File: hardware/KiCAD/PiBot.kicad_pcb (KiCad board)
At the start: 2 copper layers, 112 x 87 mm, 179 parts, among them P1 BREAKOUT, P10 BREAKOUT, P11 BREAKOUT, P12 BREAKOUT, P2 CONN_02X05, P3 I2C_EXPANSION, P4 SPI_EXPANSION, P5 Feather-Adaper, P6 BREAKOUT, P7 BREAKOUT, P8 BREAKOUT, P9 BREAKOUT, SW1 SPST, SW2 SW_SPDT, SW3 SW_SPDT, SW4 SW_SPDT, SW5 SW_SPDT, U1 DMG2302U, U10 AH3772, U11 AH3772, U12 AH3772, U13 BH1745NUC, U14 BH1745NUC, U15 L3GD20H, U16 LSM303DLHCTR, U17 N-FET, U2 MKL03ZxxVFK4, U3 N-FET, U4 TPS63060, U5 MC33926PNB, U6 MC33926PNB, U7 Motor, U8 Motor, U9 AH3772

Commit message: Inital routing done!!!!!
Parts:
- C36, C37, C39, C4, C40, C41, C42, C43, C44, C45, C46, C47, C48, C5, C6, C7, C8, D3, D5, D7, JP2, JP3, PTC1, R10, R24, R29, R31, R4, R5, R7, R9, TP1, TP11, TP13, TP14, TP15, TP19, TP23, TP25, TP29, TP3, TP35, TP39, TP41, TP43, TP45, TP47, TP49, TP5, TP7, TP8, TP9, U13, U14, U15, U16, U2: moved to B.Cu
- moved C35 141.5 mm to (170.4, 111.3)
- moved TP7 137.1 mm to (136.8, 146.0)
- moved C33 136.3 mm to (170.4, 113.1)
- moved TP35 133.4 mm to (143.3, 128.6)
- moved TP13 132.3 mm to (147.1, 146.0)
- moved TP45 130.6 mm to (164.9, 132.0)
- moved C29 129.2 mm to (170.4, 114.3)
- moved TP49 125.8 mm to (150.3, 119.1)
- moved TP1 123.0 mm to (143.4, 146.1)
- moved TP37 116.9 mm to (125.4, 68.9)
- moved R24 111.7 mm to (152.6, 100.1), turned to 270 degrees
- moved R4 105.2 mm to (168.8, 49.3), turned to 180 degrees
- moved TP14 104.7 mm to (146.7, 135.3)
- moved TP3 102.5 mm to (163.3, 112.9)
- moved C32 101.6 mm to (121.0, 114.1), turned to 180 degrees
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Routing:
- net +3V3: track 181.6 -> 389.8 mm, vias 4 -> 13
- net SDA: track 0.00 -> 160.2 mm, vias 0 -> 9
- net SCL: track 0.00 -> 154.2 mm, vias 0 -> 7
- net PG: track 0.07 -> 143.0 mm, vias 0 -> 5
- net ~MotorR_D: track 0.00 -> 94.6 mm, vias 0 -> 5
- net rear_bumper: track 2.28 -> 92.3 mm, vias 0 -> 4
- net FB_L: track 0.00 -> 87.5 mm, vias 0 -> 6
- net front_bumper: track 0.00 -> 83.7 mm
- net ~MotorL_D: track 0.00 -> 82.6 mm, vias 0 -> 7
- net left_encB: track 3.50 -> 83.0 mm, vias 0 -> 6
- net right_encA: track 4.27 -> 80.9 mm, vias 0 -> 2
- net MotorL_Inv: track 0.00 -> 75.8 mm, vias 0 -> 6
- net left_encA: track 3.50 -> 78.5 mm, vias 0 -> 6
- net Net-(R29-Pad1): track 0.00 -> 74.7 mm
- net right_encB: track 4.05 -> 76.9 mm, vias 0 -> 6
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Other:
- board size 112 x 87 mm -> 112 x 117 mm

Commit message: Start of relayout
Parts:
- moved TP45 151.1 mm to (281.2, 35.6)
- moved TP3 142.9 mm to (276.3, 25.5)
- moved R24 135.5 mm to (262.5, 20.9)
- moved R20 133.8 mm to (276.4, 22.9)
- moved C21 133.5 mm to (276.3, 21.4)
- moved D12 133.1 mm to (276.1, 19.8)
- moved U6 132.2 mm to (269.7, 22.8)
- moved R18 132.1 mm to (274.4, 16.9)
- moved C35 131.5 mm to (273.4, 29.5)
- moved TP9 131.3 mm to (275.6, 37.1)
- moved C33 131.3 mm to (273.3, 31.5)
- moved C29 131.2 mm to (273.5, 33.1)
- moved R22 130.7 mm to (264.0, 20.8)
- moved TP19 130.4 mm to (265.5, 32.3)
- moved C18 129.9 mm to (263.6, 27.4)
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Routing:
- net +3V3: track 389.8 -> 0.00 mm, vias 13 -> 0
- net +BATT: track 243.1 -> 0.00 mm, vias 18 -> 0
- net GNDPWR: track 171.4 -> 0.00 mm, vias 8 -> 0
- net SDA: track 160.2 -> 0.00 mm, vias 9 -> 0
- net SCL: track 154.2 -> 0.00 mm, vias 7 -> 0
- net +5V: track 154.2 -> 0.00 mm, vias 4 -> 0
- net PG: track 143.0 -> 0.00 mm, vias 5 -> 0
- net ~MotorSF: track 118.1 -> 0.00 mm, vias 6 -> 0
- net ~MotorR_D: track 94.6 -> 0.00 mm, vias 5 -> 0
- net rear_bumper: track 92.3 -> 0.00 mm, vias 4 -> 0
- net FB_L: track 87.5 -> 0.00 mm, vias 6 -> 0
- net front_bumper: track 83.7 -> 0.00 mm
- net left_encB: track 83.0 -> 0.00 mm, vias 6 -> 0
- net ~MotorL_D: track 82.6 -> 0.00 mm, vias 7 -> 0
- net right_encA: track 80.9 -> 0.00 mm, vias 2 -> 0
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- removed copper zone on B.Cu, net GND
- removed copper zone on F.Cu, net GND
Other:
- board size 112 x 117 mm -> 64 x 123 mm

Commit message: Headway on schematic layout
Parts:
- removed P1: BREAKOUT, Pin_Headers:Pin_Header_Straight_1x07_Pitch2.54mm
- removed P10, P6, P9: BREAKOUT, Pin_Headers:Pin_Header_Straight_1x01_Pitch2.54mm
- removed P11, P8: BREAKOUT, Pin_Headers:Pin_Header_Straight_2x01_Pitch2.54mm
- removed P12: BREAKOUT, Pin_Headers:Pin_Header_Straight_1x03_Pitch2.54mm
- removed P4: SPI_EXPANSION, Pin_Headers:Pin_Header_Straight_1x03_Pitch2.54mm
- removed P7: BREAKOUT, Pin_Headers:Pin_Header_Straight_1x05_Pitch2.54mm
- added DRDY1: TEST, Measurement_Points:Measurement_Point_Round-SMD-Pad_Small, F.Cu at (148.0, 153.0)
- added INT1: TEST, Measurement_Points:Measurement_Point_Round-SMD-Pad_Small, F.Cu at (142.0, 153.0)
- added INT2: TEST, Measurement_Points:Measurement_Point_Round-SMD-Pad_Small, F.Cu at (145.0, 153.0)
- added TP10: TEST, Measurement_Points:Measurement_Point_Round-SMD-Pad_Small, F.Cu at (164.5, 163.8)
- added TP12: TEST, Measurement_Points:Measurement_Point_Round-SMD-Pad_Small, F.Cu at (142.5, 164.8)
- added TP4: TEST, Measurement_Points:Measurement_Point_Round-SMD-Pad_Small, F.Cu at (160.5, 161.8)
- added TP6: TEST, Measurement_Points:Measurement_Point_Round-SMD-Pad_Small, F.Cu at (148.5, 163.5)
- R8: moved to B.Cu
- moved TP33 135.9 mm to (126.0, 142.5)
- moved C45 134.1 mm to (149.9, 151.5), turned to 180 degrees
- moved R5 133.9 mm to (159.4, 148.2), turned to 90 degrees
- moved C44 133.4 mm to (151.2, 149.5), turned to 180 degrees
- moved U13 132.8 mm to (181.0, 150.5)
- moved U14 132.5 mm to (129.0, 150.5)
- moved C48 132.1 mm to (158.5, 153.1)
- moved U16 132.0 mm to (155.0, 151.5)
- moved R4 131.8 mm to (158.0, 146.6), turned to 0 degrees
- moved C39 131.7 mm to (179.5, 154.0)
- moved C36 130.7 mm to (125.5, 149.0)
- moved TP31 130.4 mm to (126.0, 136.5)
- moved C47 130.2 mm to (151.1, 153.5), turned to 180 degrees
- moved TP27 128.3 mm to (126.0, 139.5)
- moved R8 127.4 mm to (126.9, 134.7), turned to 270 degrees
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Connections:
- P2 pad 7: Net-(P2-Pad7) -> (no net)
- P2 pad 8: Net-(P2-Pad8) -> (no net)
- P5 pad 1: Net-(P5-Pad1) -> (no net)
- P5 pad 10: Net-(P1-Pad1) -> (no net)
- P5 pad 14: Net-(P5-Pad14) -> (no net)
- P5 pad 15: Net-(P5-Pad15) -> (no net)
- P5 pad 20: Net-(P5-Pad20) -> (no net)
- P5 pad 21: Net-(P5-Pad21) -> (no net)
- P5 pad 22: Net-(P5-Pad22) -> (no net)
- P5 pad 23: Net-(P5-Pad23) -> (no net)
- P5 pad 24: Net-(P5-Pad24) -> (no net)
- P5 pad 26: Net-(P5-Pad26) -> (no net)
- P5 pad 4: Net-(P1-Pad7) -> (no net)
- P5 pad 5: Net-(P1-Pad6) -> (no net)
- P5 pad 6: Net-(P1-Pad5) -> (no net)
- P5 pad 7: Net-(P1-Pad4) -> (no net)
- P5 pad 8: Net-(P1-Pad3) -> (no net)
- P5 pad 9: Net-(P1-Pad2) -> (no net)
- SD1 pad PIN8: Net-(SD1-PadPIN8) -> (no net)
- SW2 pad 1: Net-(SW2-Pad1) -> (no net)
- SW3 pad 1: Net-(SW3-Pad1) -> (no net)
- SW4 pad 1: Net-(SW4-Pad1) -> (no net)
- SW5 pad 1: Net-(SW5-Pad1) -> (no net)
- TP25 pad 1: MotorR_Inv -> (no net)
- U13 pad 8: Net-(U13-Pad8) -> (no net)
- U14 pad 8: Net-(U14-Pad8) -> (no net)
- U16 pad 8: Net-(U16-Pad8) -> (no net)
- U5 pad 17: Net-(U5-Pad17) -> (no net)
- U5 pad 25: Net-(U5-Pad25) -> (no net)
- U5 pad 3: Net-(U5-Pad3) -> (no net)
- U5 pad 9: Net-(U5-Pad9) -> (no net)
- U6 pad 17: Net-(U6-Pad17) -> (no net)
- U6 pad 25: Net-(U6-Pad25) -> (no net)
- U6 pad 3: Net-(U6-Pad3) -> (no net)
- U6 pad 7: /motors/MotorR_Inv -> (no net)
- U6 pad 9: Net-(U6-Pad9) -> (no net)
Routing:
- net SCK: track 0.00 -> 27.5 mm, vias 0 -> 3
- net MISO: track 0.00 -> 24.6 mm, vias 0 -> 3
- net MOSI: track 0.00 -> 23.1 mm, vias 0 -> 3
- net Net-(DRDY1-Pad1): track 0.00 -> 21.1 mm, vias 0 -> 1
- net Net-(JP1-Pad1): track 0.00 -> 17.9 mm, vias 0 -> 1
- net Net-(SD1-PadPIN1): track 0.00 -> 17.8 mm, vias 0 -> 2
- net Net-(INT1-Pad1): track 0.00 -> 14.7 mm, vias 0 -> 1
- net Net-(INT2-Pad1): track 0.00 -> 10.9 mm, vias 0 -> 1
- net +3V3: track 0.00 -> 9.91 mm
- net SD_CS: track 0.00 -> 7.12 mm, vias 0 -> 2
- net Net-(C48-Pad1): track 0.00 -> 2.52 mm
- net Net-(C48-Pad2): track 0.00 -> 2.52 mm
- net Net-(C44-Pad1): track 0.00 -> 2.30 mm
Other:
- net class any added: clearance 0, trace_width 0.3, via_dia 0.6, via_drill 0.4
- board text added: "MISO"
- board text added: "MOSI"
- board text added: "SCK"
- board text added: "SD_CS"

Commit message: Lay out encoders and begin motor drive
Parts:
- C24, C25, C28, C29, C30, C31, C32, C33, C34, C35, U5, U6: moved to B.Cu
- JP10, JP11, JP12, JP13, JP14, JP7, JP8, JP9: moved to F.Cu
- moved C27 132.6 mm to (155.0, 40.5), turned to 90 degrees
- moved JP9 129.7 mm to (157.0, 38.0), turned to 270 degrees
- moved JP14 126.1 mm to (157.0, 40.5), turned to 90 degrees
- moved R27 121.9 mm to (156.0, 42.5)
- moved R25 121.4 mm to (156.0, 52.5)
- moved JP10 121.3 mm to (157.0, 57.0)
- moved U10 120.9 mm to (157.0, 50.0)
- moved JP12 120.8 mm to (157.0, 54.5), turned to 270 degrees
- moved U5 119.6 mm to (129.5, 47.5), turned to 180 degrees
- moved U12 118.4 mm to (157.0, 45.0)
- moved C23 114.6 mm to (163.5, 40.5), turned to 0 degrees
- moved C31 113.5 mm to (164.5, 47.0), turned to 270 degrees
- moved C25 112.5 mm to (163.0, 47.0), turned to 270 degrees
- moved JP13 112.3 mm to (153.0, 40.5), turned to 90 degrees
- moved JP7 106.8 mm to (153.0, 38.0)
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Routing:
- net +3V3: track 9.91 -> 47.6 mm, vias 0 -> 2
- net Net-(BT3-Pad2): track 0.00 -> 30.2 mm
- net Net-(BT2-Pad2): track 0.00 -> 30.2 mm
- net Net-(BT1-Pad2): track 0.00 -> 30.2 mm
- net /power/BATT_V+_TERM: track 0.00 -> 26.0 mm
- net Net-(C22-Pad2): track 0.00 -> 21.0 mm
- net Net-(C23-Pad2): track 0.00 -> 21.0 mm
- net Net-(JP8-Pad2): track 0.00 -> 17.2 mm, vias 0 -> 2
- net Net-(JP7-Pad1): track 0.00 -> 15.6 mm, vias 0 -> 2
- net Net-(JP9-Pad1): track 0.00 -> 14.6 mm, vias 0 -> 2
- net Net-(JP10-Pad2): track 0.00 -> 11.2 mm, vias 0 -> 2
- net Net-(R32-Pad1): track 0.00 -> 10.5 mm
- net /power/BATT_GND_TERM: track 0.00 -> 7.62 mm
- net Net-(C23-Pad1): track 0.00 -> 5.86 mm
- net Net-(C22-Pad1): track 0.00 -> 5.86 mm
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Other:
- net class any removed

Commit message: Lay out motor drivers
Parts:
- C20, C21, D11, D12, JP5, R17, R18, TP11, TP19, TP3, TP39, TP9: moved to F.Cu
- moved JP17 169.3 mm to (164.0, 69.0), turned to 90 degrees
- moved TP9 108.1 mm to (167.5, 35.0)
- moved TP11 105.6 mm to (165.0, 35.0)
- moved TP3 91.7 mm to (145.0, 35.0)
- moved TP19 60.6 mm to (213.5, 101.5)
- moved D12 40.2 mm to (174.5, 60.0), turned to 270 degrees
- moved R19 39.9 mm to (142.5, 51.5), turned to 0 degrees
- moved R18 38.4 mm to (176.5, 60.0), turned to 270 degrees
- moved R20 37.8 mm to (173.5, 51.0), turned to 0 degrees
- moved R22 37.2 mm to (165.0, 59.5), turned to 270 degrees
- moved C20 36.8 mm to (147.0, 60.0), turned to 270 degrees
- moved C21 36.1 mm to (178.5, 60.0), turned to 270 degrees
- moved R21 34.2 mm to (134.0, 59.0)
- moved JP5 34.0 mm to (149.5, 60.0), turned to 90 degrees
- moved C18 33.1 mm to (165.0, 51.5)
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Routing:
- net Net-(C22-Pad2): track 21.0 -> 153.6 mm
- net Net-(C23-Pad1): track 5.86 -> 121.4 mm
- net GNDPWR: track 0.00 -> 82.3 mm
- net PG: track 0.00 -> 69.2 mm, vias 0 -> 4
- net +BATT: track 0.00 -> 68.4 mm
- net Motor_In1: track 0.00 -> 66.0 mm, vias 0 -> 4
- net Motor_In2: track 0.00 -> 63.1 mm, vias 0 -> 4
- net ~MotorSF: track 0.00 -> 36.0 mm, vias 0 -> 4
- net Net-(C23-Pad2): track 21.0 -> 52.9 mm
- net Net-(C22-Pad1): track 5.86 -> 36.0 mm
- net Net-(C20-Pad1): track 0.00 -> 15.3 mm, vias 0 -> 1
- net Net-(C21-Pad1): track 0.00 -> 12.7 mm, vias 0 -> 1
- net Net-(C18-Pad2): track 0.00 -> 3.43 mm
- net Net-(C19-Pad2): track 0.00 -> 2.72 mm
- net Net-(R22-Pad1): track 0.00 -> 2.09 mm
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- added copper zone on B.Cu, net +BATT
- added copper zone on B.Cu, net GNDPWR
- added copper zone on B.Cu, net Net-(C22-Pad1)
- added copper zone on B.Cu, net Net-(C22-Pad2)
- added copper zone on B.Cu, net Net-(C23-Pad1)
- added copper zone on B.Cu, net Net-(C23-Pad2)

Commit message: Layout PSU
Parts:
- moved D9 194.8 mm to (184.0, 82.5), turned to 270 degrees
- moved JP18 190.8 mm to (176.5, 71.0), turned to 270 degrees
- moved JP4 182.8 mm to (176.5, 76.5), turned to 270 degrees
- moved D8 181.6 mm to (184.0, 97.5)
- moved U17 167.1 mm to (172.5, 72.5), turned to 0 degrees
- moved R32 161.2 mm to (168.5, 72.5), turned to 90 degrees
- moved U3 159.1 mm to (172.5, 77.5), turned to 0 degrees
- moved C9 158.1 mm to (172.5, 75.0), turned to 0 degrees
- moved C10 156.1 mm to (165.5, 77.5)
- moved D10 155.7 mm to (168.5, 77.5), turned to 90 degrees
- moved C11 149.2 mm to (163.5, 114.0), turned to 270 degrees
- moved R11 140.7 mm to (167.5, 112.5), turned to 180 degrees
- moved C12 123.6 mm to (160.0, 114.0), turned to 270 degrees
- moved L1 119.5 mm to (154.5, 109.5), turned to 180 degrees
- moved R13 115.6 mm to (154.5, 118.0), turned to 0 degrees
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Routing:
- net Net-(R32-Pad1): track 10.5 -> 75.0 mm, vias 0 -> 1
- net /power/BATT_V+_TERM: track 26.0 -> 89.4 mm, vias 0 -> 2
- net /power/BATT_GND_TERM: track 7.62 -> 34.0 mm
- net /power/PSU_VOUT: track 0.00 -> 15.2 mm
- net +BATT: track 68.4 -> 82.6 mm
- net Net-(C9-Pad2): track 0.00 -> 11.8 mm
- net Net-(D8-Pad2): track 0.00 -> 11.0 mm
- net /power/PSU_FB: track 0.00 -> 8.06 mm
- net Net-(L1-Pad2): track 0.00 -> 3.64 mm
- net /power/PSU_IND: track 0.00 -> 3.64 mm
- net Net-(R12-Pad2): track 0.00 -> 2.78 mm
- added copper zone on B.Cu, net /power/PSU_VOUT
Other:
- net class Default: trace_width 0.4 -> 0.6

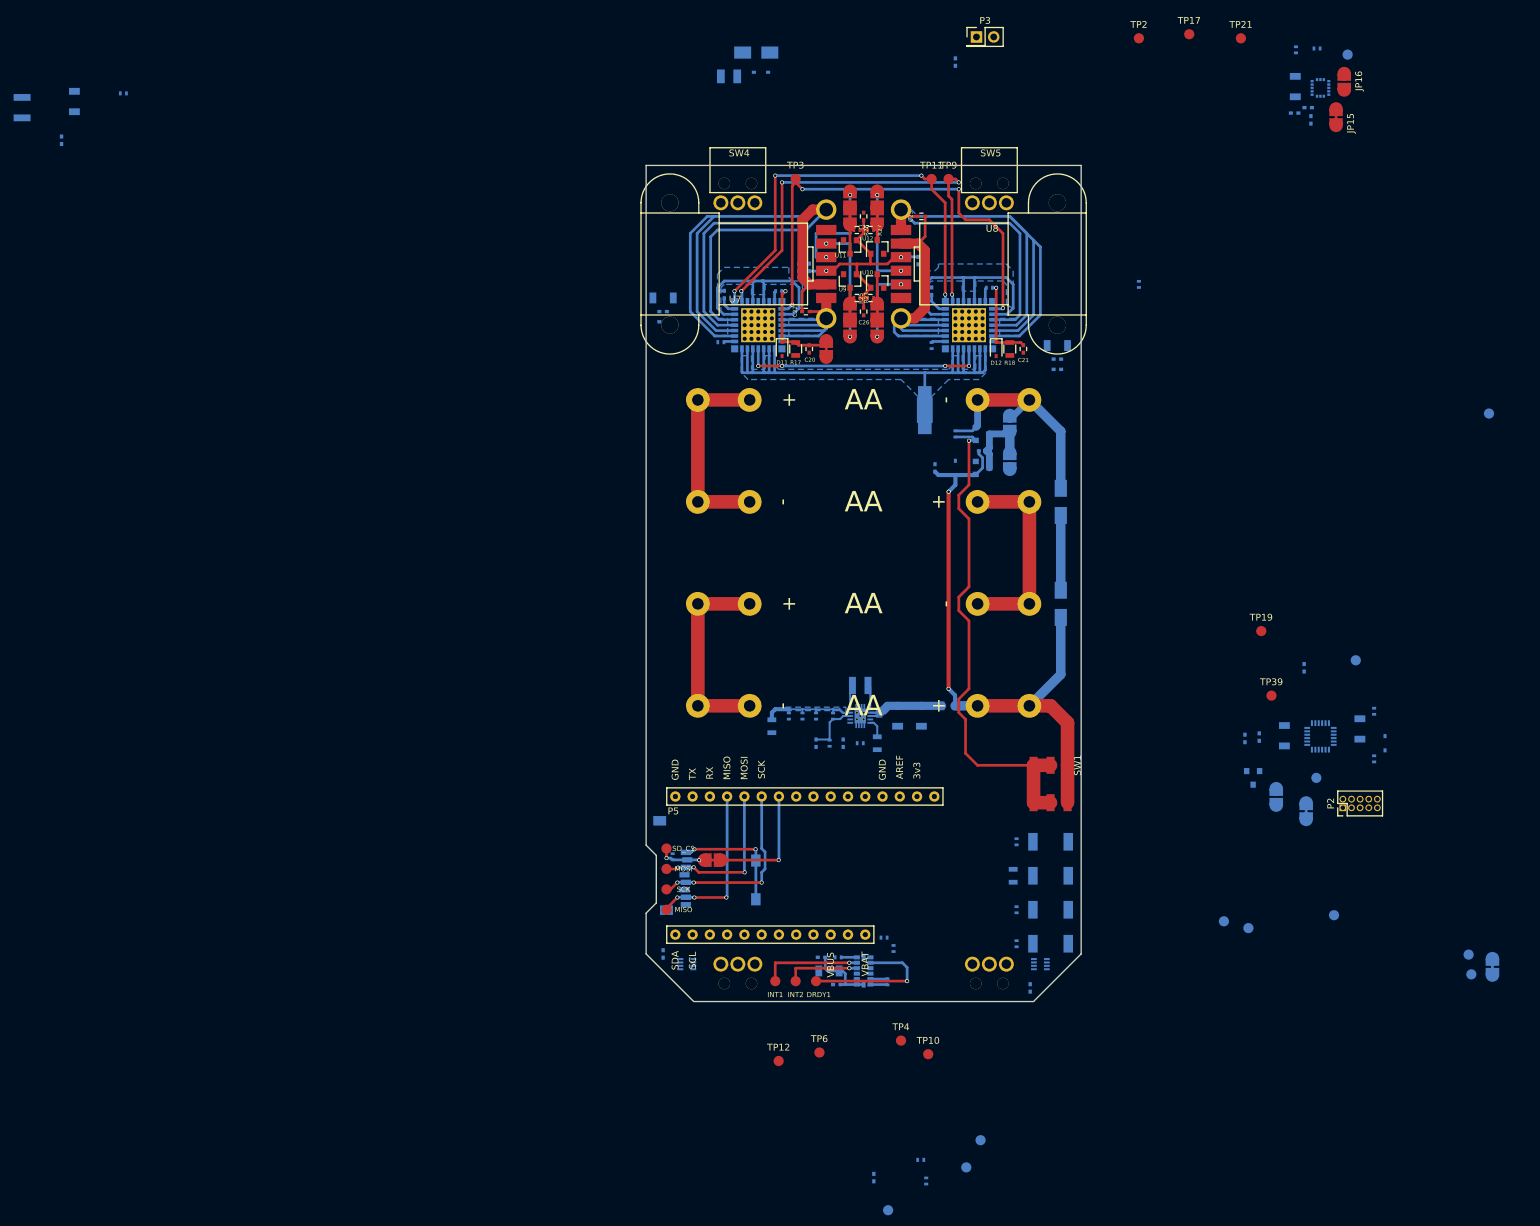
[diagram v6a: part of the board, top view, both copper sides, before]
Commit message: Finish part placement
Now just to route everything :P
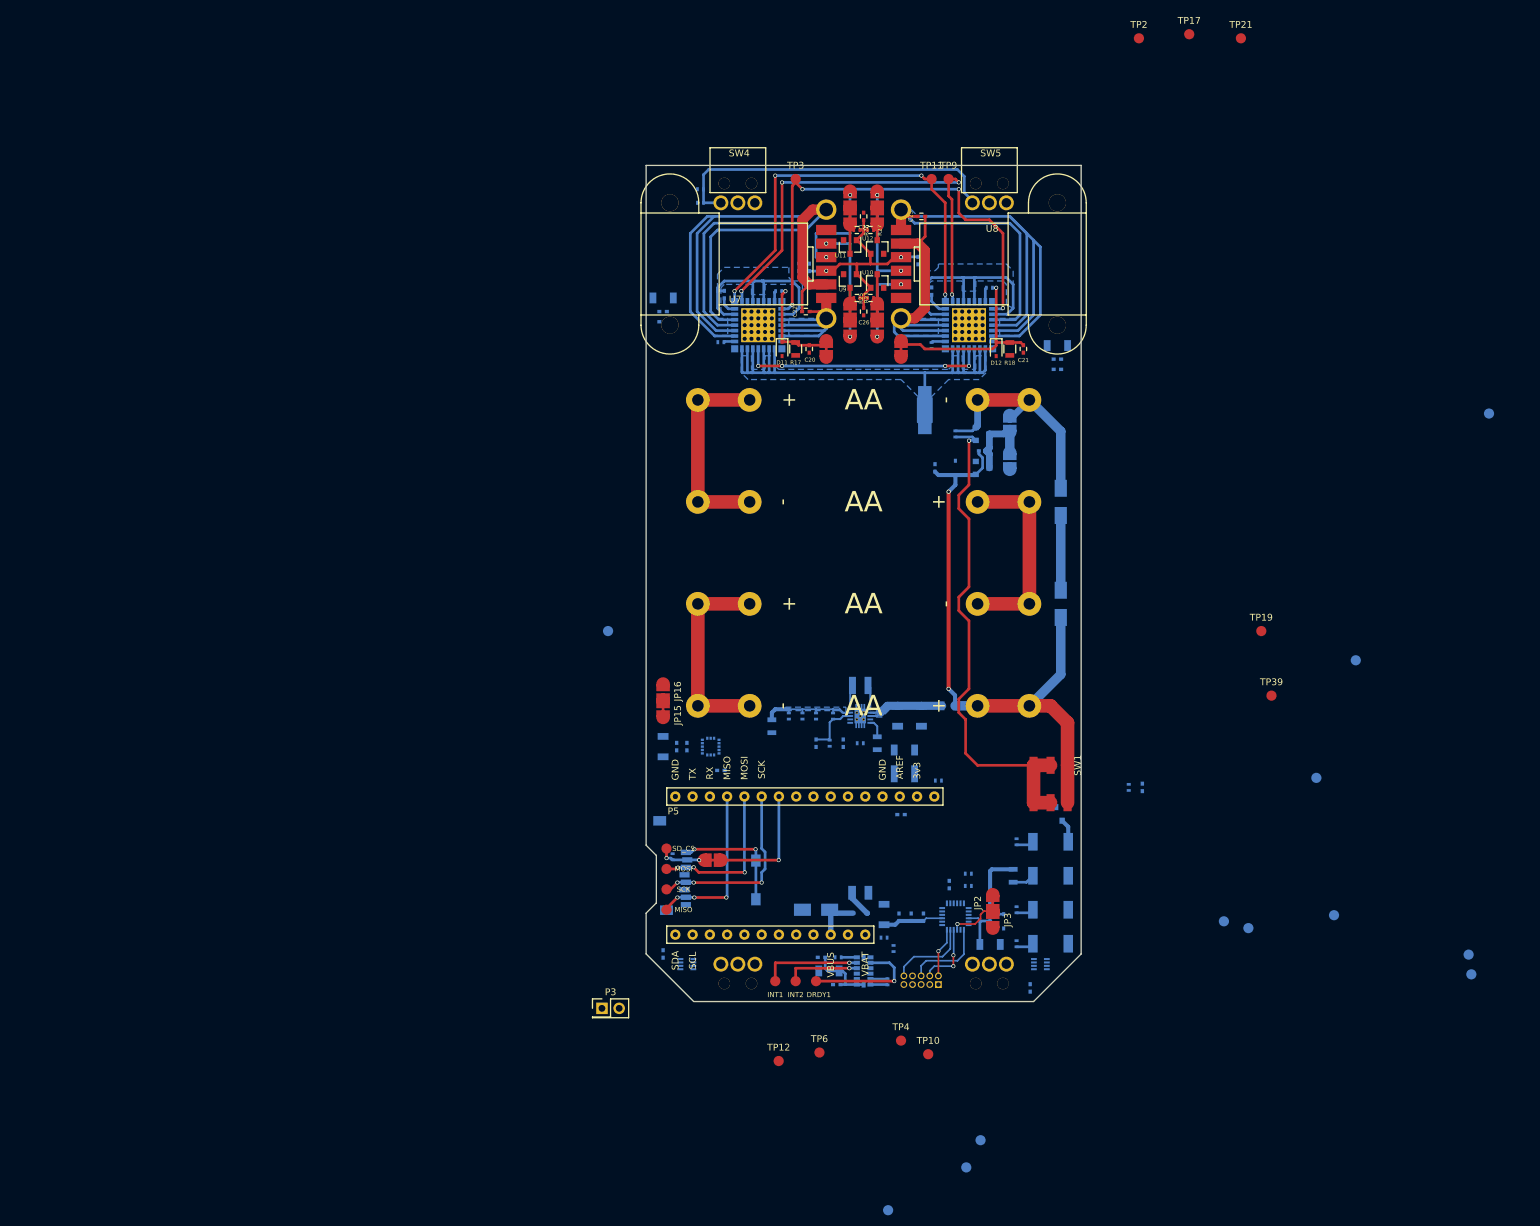
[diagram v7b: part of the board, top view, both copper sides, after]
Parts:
- JP2, JP3, JP6: moved to F.Cu
- P2: moved to B.Cu
- moved C1 162.6 mm to (161.0, 122.5), turned to 180 degrees
- moved C3 158.4 mm to (160.5, 128.5), turned to 180 degrees
- moved R7 156.8 mm to (166.0, 123.5), turned to 0 degrees
- moved C2 155.0 mm to (161.0, 119.0), turned to 180 degrees
- moved P3 153.2 mm to (116.5, 157.0)
- moved TP47 137.9 mm to (117.4, 101.5)
- moved JP16 134.6 mm to (125.5, 110.5)
- moved C40 134.5 mm to (125.5, 118.5)
- moved U15 132.0 mm to (132.5, 118.5)
- moved JP15 131.9 mm to (125.5, 113.0)
- moved C42 131.1 mm to (129.0, 118.5), turned to 270 degrees
- moved C43 130.2 mm to (127.5, 118.5), turned to 270 degrees
- moved C41 129.2 mm to (134.0, 122.0), turned to 0 degrees
- moved D5 126.4 mm to (148.0, 142.5)
- moved JP6 125.8 mm to (160.5, 60.0), turned to 90 degrees
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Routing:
- net Net-(R29-Pad1): track 0.00 -> 50.2 mm
- net Net-(C21-Pad1): track 12.7 -> 27.7 mm
- net SWO: track 0.00 -> 12.1 mm
- net RESET: track 0.00 -> 12.1 mm
- net SWCLK: track 0.00 -> 9.88 mm, vias 0 -> 2
- net /VBATT_MONITOR: track 0.00 -> 9.77 mm
- net +3V3: track 47.6 -> 56.6 mm
- net +BATT: track 82.6 -> 91.4 mm
- net SWDIO: track 0.00 -> 7.30 mm, vias 0 -> 1
- net /I2C_LSB_BIT: track 0.00 -> 7.21 mm, vias 0 -> 1
- net /F_VBUS: track 0.00 -> 6.93 mm
- net Net-(D3-Pad2): track 0.00 -> 3.96 mm
- net Net-(DRDY1-Pad1): track 21.1 -> 17.3 mm
- net Net-(D6-Pad1): track 0.00 -> 3.47 mm
- net Net-(D4-Pad2): track 0.00 -> 3.29 mm
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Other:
- net class Default: trace_width 0.6 -> 0.4
